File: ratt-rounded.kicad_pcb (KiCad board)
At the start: 2 copper layers, 40.6 x 30.7 mm, 35 parts, among them J1 Conn_01x04_Male, J2 Conn_01x04_Male, Q1 2N5457, U1 LM308N

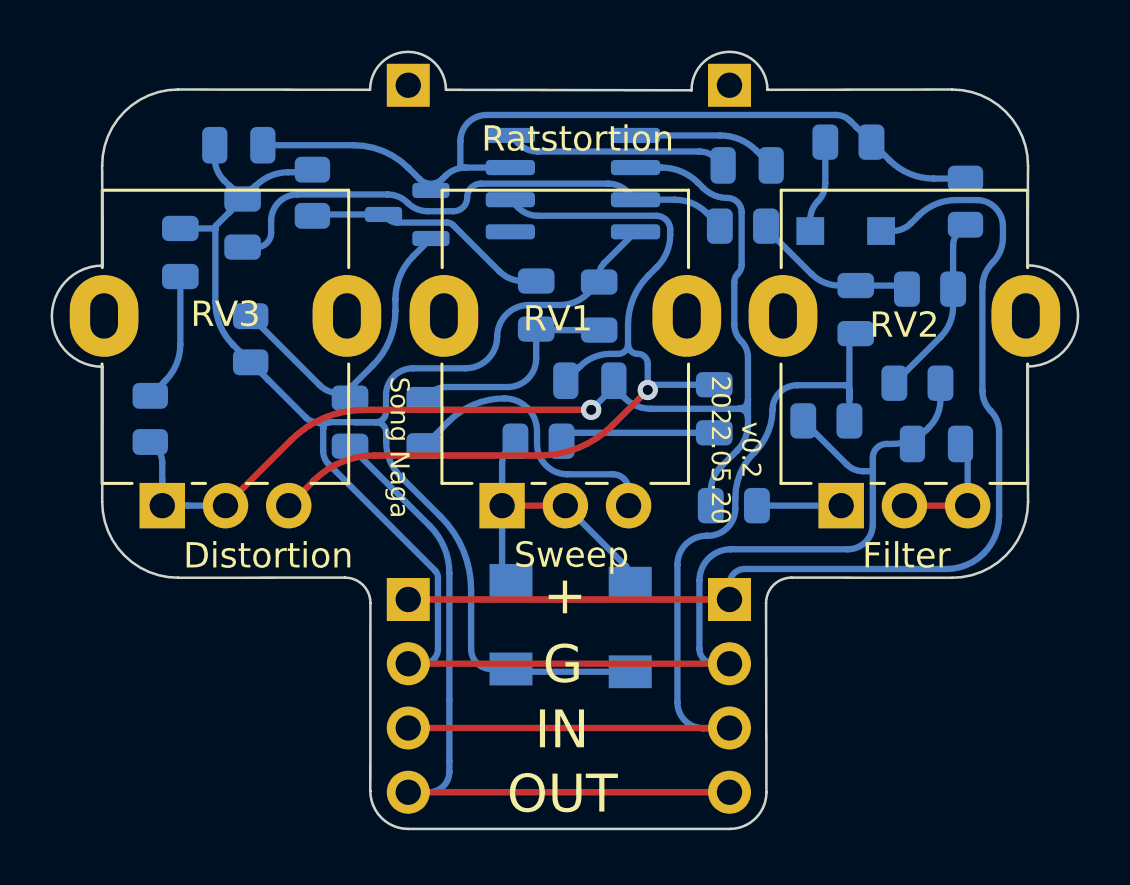
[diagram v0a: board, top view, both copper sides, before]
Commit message: updated rotation of pots.
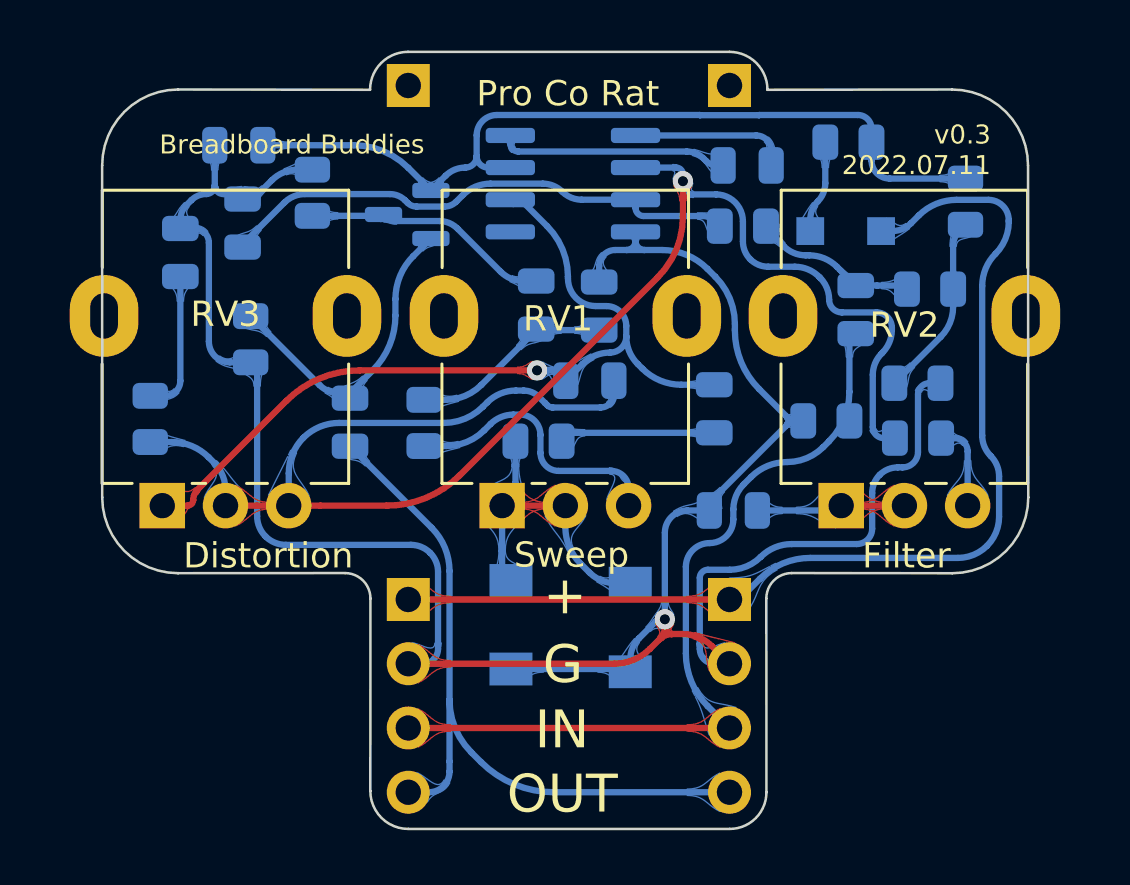
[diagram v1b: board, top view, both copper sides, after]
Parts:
- removed REF1, REF2: PinHeader_1x01_P2.54mm_Vertical, Connector_PinHeader_2.54mm:PinHeader_1x01_P2.54mm_Vertical
- added G1: LOGO, LOGO, B.Cu at (35.8, 51.8)
- added J3: Conn_01x01_Male, Connector_PinSocket_2.54mm:PinSocket_1x01_P2.54mm_Vertical, B.Cu at (29.4, 24.2)
- added J4: Conn_01x01_Male, Connector_PinSocket_2.54mm:PinSocket_1x01_P2.54mm_Vertical, B.Cu at (42.1, 24.2)
- moved C10 8.45 mm to (42.3, 41.0)
- moved R8 7.75 mm to (49.6, 38.2)
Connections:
- RV2 pad 1: Net-(R8-Pad1) -> Net-(C10-Pad1)
- RV2 pad 3: Net-(C10-Pad1) -> Net-(R8-Pad1)
- RV3 pad 1: Net-(C8-Pad1) -> Net-(C2-Pad1)
- RV3 pad 3: Net-(C2-Pad1) -> Net-(C8-Pad1)
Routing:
- net Net-(C8-Pad1): track 45.8 -> 65.3 mm
- net INPUT: track 36.0 -> 32.4 mm
- net Net-(C2-Pad1): track 35.6 -> 33.5 mm
- net GND: track 102.7 -> 101.8 mm, vias 0 -> 1
- net Net-(C10-Pad1): track 5.03 -> 5.88 mm
- net VA: track 32.8 -> 33.7 mm
- net Net-(C3-Pad1): track 8.89 -> 8.05 mm
- net Net-(C4-Pad1): track 21.4 -> 20.8 mm
- net Net-(C11-Pad1): track 5.11 -> 5.63 mm
- net Net-(D1-Pad2): track 12.4 -> 12.9 mm
- net Net-(C6-Pad2): track 5.76 -> 6.27 mm
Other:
- board size 40.6 x 30.7 mm -> 36.6 x 30.7 mm
- board text added: "Breadboard Buddies"
- board text added: "Pro Co Rat"
- board text added: "v0.3 2022.07.11"
- board text removed: "Ratstortion"
- board text removed: "Song Naga"
- board text removed: "v0.2 2022.05.20"
